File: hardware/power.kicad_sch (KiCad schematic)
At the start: 34 parts, among them U3 TI LMR51430YFDDCR, U4 TI LMR51430YFDDCR, U5 TPS2116DRLR, U6 NCV8187AMT180TAG, U7 LP5912-3.3DRVR

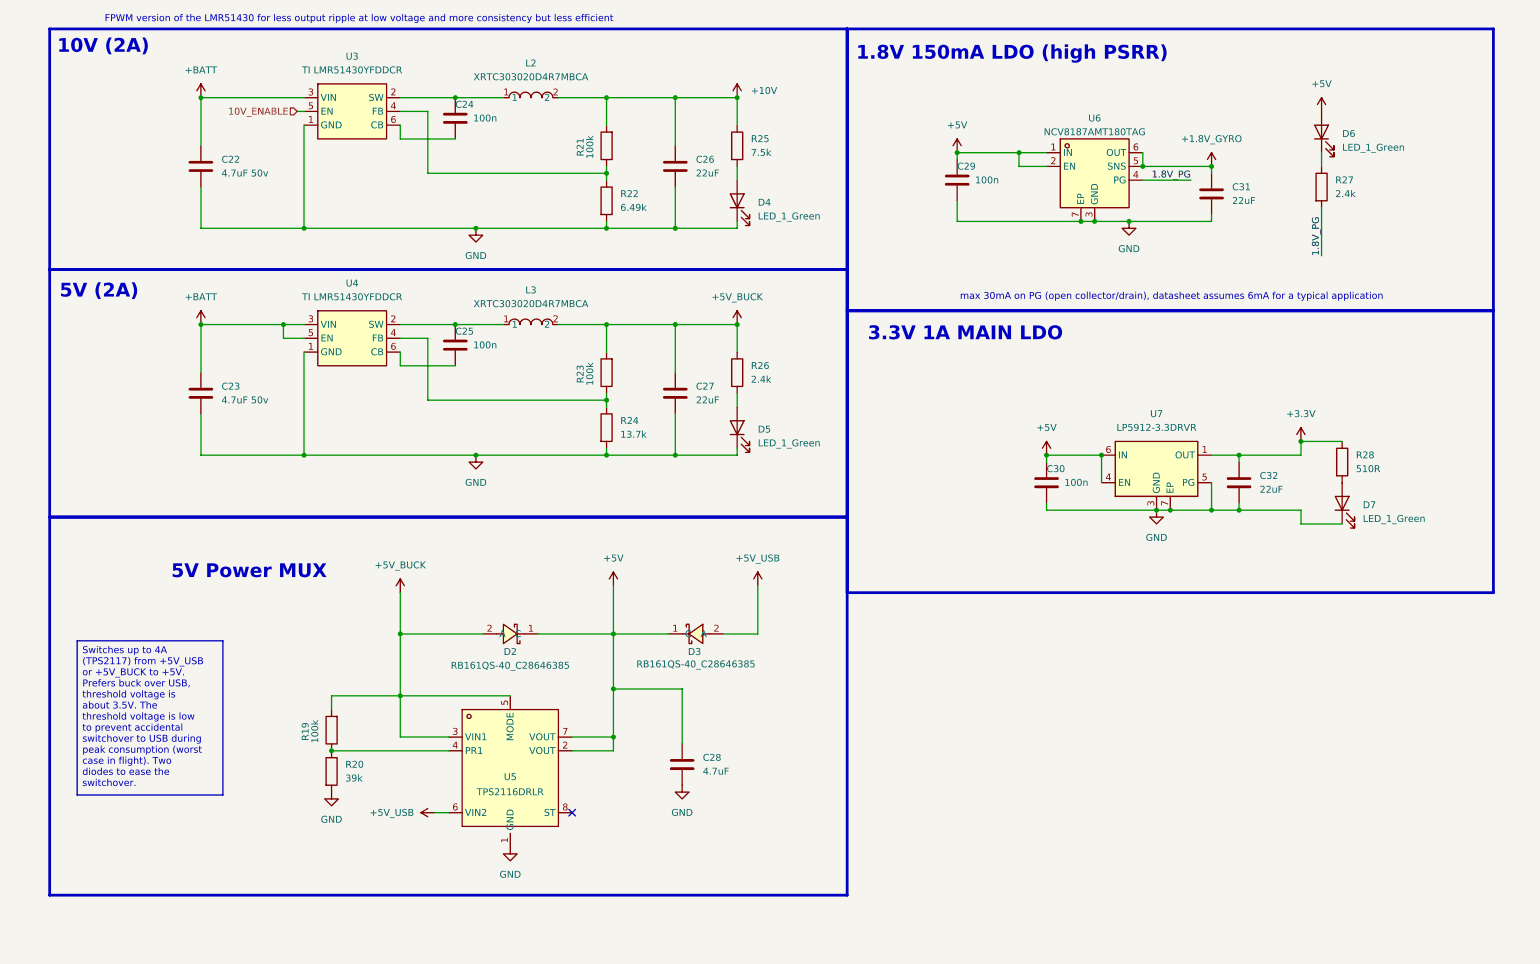
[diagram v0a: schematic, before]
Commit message: Rev 2: finalize schematic + PCB for fabrication
Rev 2 change list implemented; on-canvas design annotations added across all
sheets (root, rp2350a, power, imu, osd, blackbox, pads). Design frozen for ordering.

Co-Authored-By: Claude Opus 4.8 (1M context) <noreply@anthropic.com>
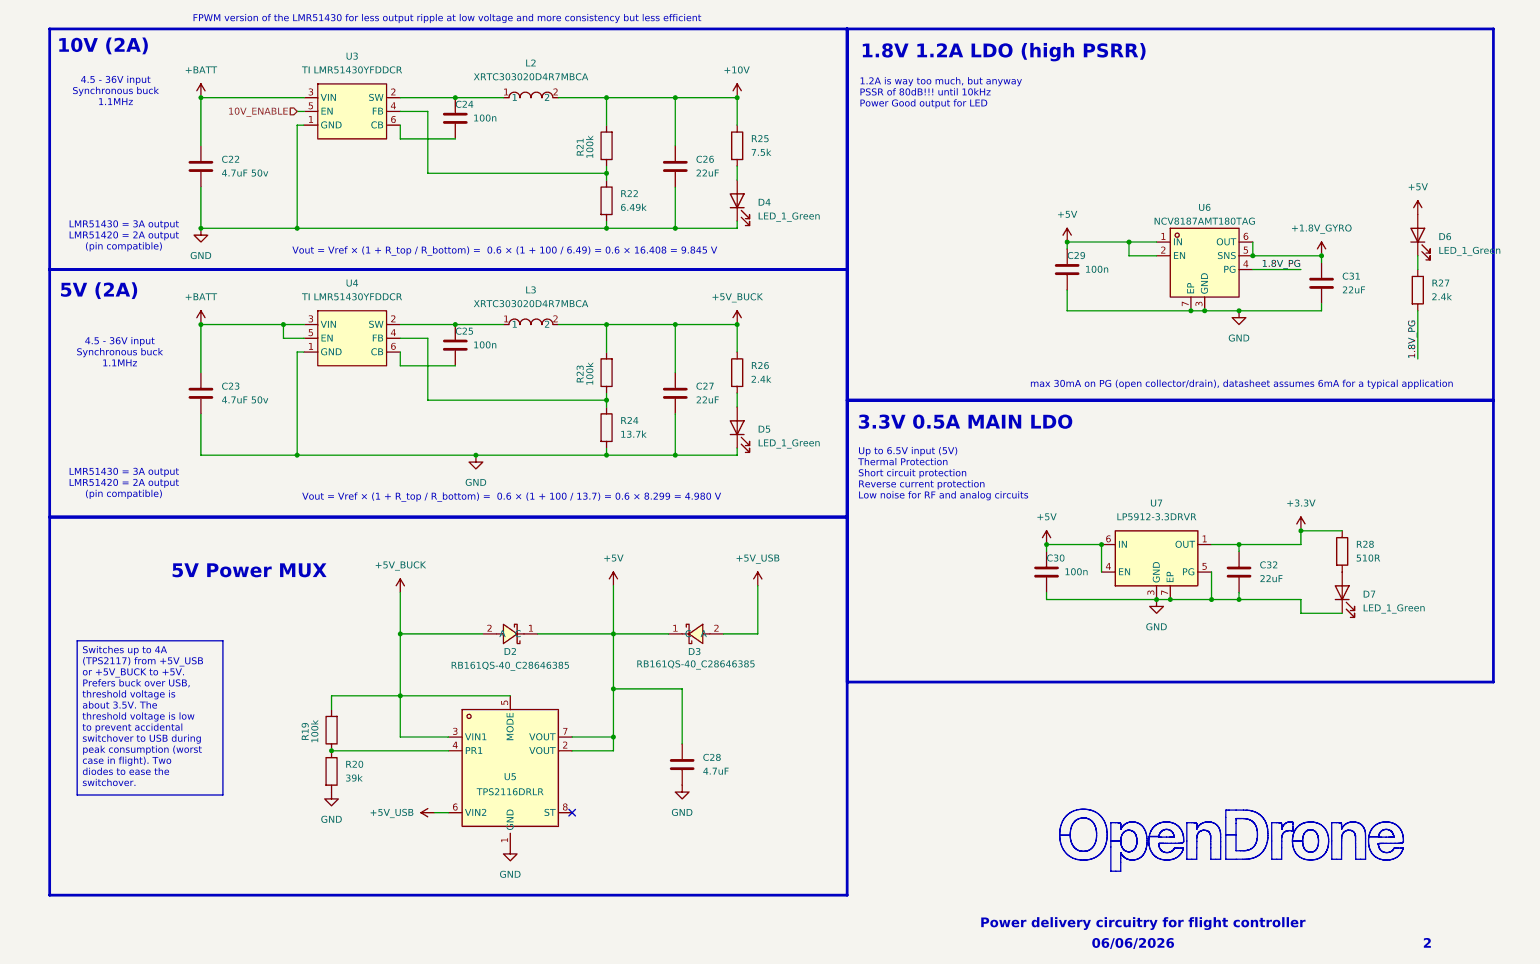
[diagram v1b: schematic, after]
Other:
- note added: "06/06/2026"
- note added: "1.2A is way too much, but anyway PSSR of 80dB!!! until 10kHz Power Good output for LED"
- note added: "1.8V 1.2A LDO (high PSRR)"
- note added: "2"
- note added: "3.3V 0.5A MAIN LDO"
- note added: "4.5 - 36V input Synchronous buck 1.1MHz"
- note added: "LMR51430 = 3A output LMR51420 = 2A output (pin compatible)"
- note added: "Power delivery circuitry for flight controller"
- note added: "Up to 6.5V input (5V) Thermal Protection Short circuit protection Reverse current protection Low noise for RF and analog circuits"
- note added: "Vout = Vref × (1 + R_top / R_bottom) = 0.6 × (1 + 100 / 13.7) = 0.6 × 8.299 = 4.980 V"
- note added: "Vout = Vref × (1 + R_top / R_bottom) = 0.6 × (1 + 100 / 6.49) = 0.6 × 16.408 = 9.845 V"
- note removed: "1.8V 150mA LDO (high PSRR)"
- note removed: "3.3V 1A MAIN LDO"
- moved on the sheet: C29, C30, C31, C32, D6, D7, R27, R28, U6, U7

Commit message: chore(bom): consolidate LCSC Part -> LCSC field across schematic, library, footprints, project
Single canonical LCSC field (was split LCSC / LCSC Part). Every part resolves to one LCSC code; netlist verified, no duplicates. Includes Rev2 re-annotation resync re-save.

Co-Authored-By: Claude Opus 4.8 (1M context) <noreply@anthropic.com>
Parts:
- D2, D3: LCSC (none) -> C28646385; LCSC Part C28646385 -> (none)
- L2, L3: LCSC (none) -> C39846837; LCSC Part C39846837 -> (none)
- U3, U4: LCSC (none) -> C5219261; LCSC Part C5219261 -> (none)
- U5: LCSC (none) -> C3235557; LCSC Part C3235557 -> (none)
- U6: LCSC (none) -> C893189; LCSC Part C893189 -> (none)
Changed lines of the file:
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@@
 			)
 		)
-		(property "LCSC Part" "C39846837"
+		(property "LCSC" "C39846837"
 			(at 104.14 46.99 0)
 			(hide yes)
@@
 			)
 		)
-		(property "LCSC Part" "C28646385"
+		(property "LCSC" "C28646385"
 			(at 134.62 146.05 0)
 			(hide yes)
@@
 			)
 		)
-		(property "LCSC Part" "C3235557"
+		(property "LCSC" "C3235557"
 			(at 100.33 170.18 0)
 			(hide yes)
@@
 			)
 		)
-		(property "LCSC Part" "C39846837"
+		(property "LCSC" "C39846837"
 			(at 104.14 88.9 0)
 			(hide yes)
@@
 			)
 		)
-		(property "LCSC Part" "C5219261"
+		(property "LCSC" "C5219261"
 			(at 71.12 52.07 0)
 			(hide yes)
@@
 			)
 		)
-		(property "LCSC Part" "C893189"
+		(property "LCSC" "C893189"
 			(at 228.6 81.28 0)
 			(hide yes)
@@
 			)
 		)
-		(property "LCSC Part" "C28646385"
+		(property "LCSC" "C28646385"
 			(at 100.33 125.73 0)
 			(hide yes)
@@
 			)
 		)
-		(property "LCSC Part" "C5219261"
+		(property "LCSC" "C5219261"
 			(at 71.12 93.98 0)
 			(hide yes)
